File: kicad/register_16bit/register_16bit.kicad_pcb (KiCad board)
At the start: 2 copper layers, 175.3 x 72.4 mm, 84 parts, among them J1 DB37_Male, U1 SN74ALVC00, U10 SN74ALVC00, U11 SN74ALVC00, U12 SN74ALVC00, U13 SN74ALVC00, U14 SN74ALVC00, U15 SN74ALVC00, U16 SN74ALVC00, U17 SN74ALVC00, U18 SN74ALVC00, U19 SN74ALVC00, U2 SN74ALVC00, U20 SN74ALVC00, U21 SN74ALVC00, U22 SN74ALVC00, U23 SN74ALVC00, U24 SN74ALVC00, U25 SN74ALVC00, U26 SN74ALVC00, U27 SN74ALVC00, U28 SN74ALVC00, U29 SN74ALVC00, U3 SN74ALVC00, U30 SN74ALVC00, U31 SN74ALVC00, U32 SN74ALVC00, U33 SN74ALVC00, U34 SN74ALVC00, U35 SN74ALVC00, U36 SN74ALVC00, U37 SN74ALVC00, U38 SN74ALVC00, U39 SN74ALVC00, U4 SN74ALVC00, U40 SN74ALVC00, U41 SN74ALVC00, U42 SN74ALVC00, U43 SN74ALVC00, U44 SN74ALVC00, U45 SN74ALVC00, U46 SN74ALVC00, U47 SN74ALVC00, U48 SN74ALVC00, U49 SN74ALVC00, U5 SN74ALVC00, U6 SN74ALVC00, U7 SN74ALVC00, U8 SN74ALVC00, U9 SN74ALVC00

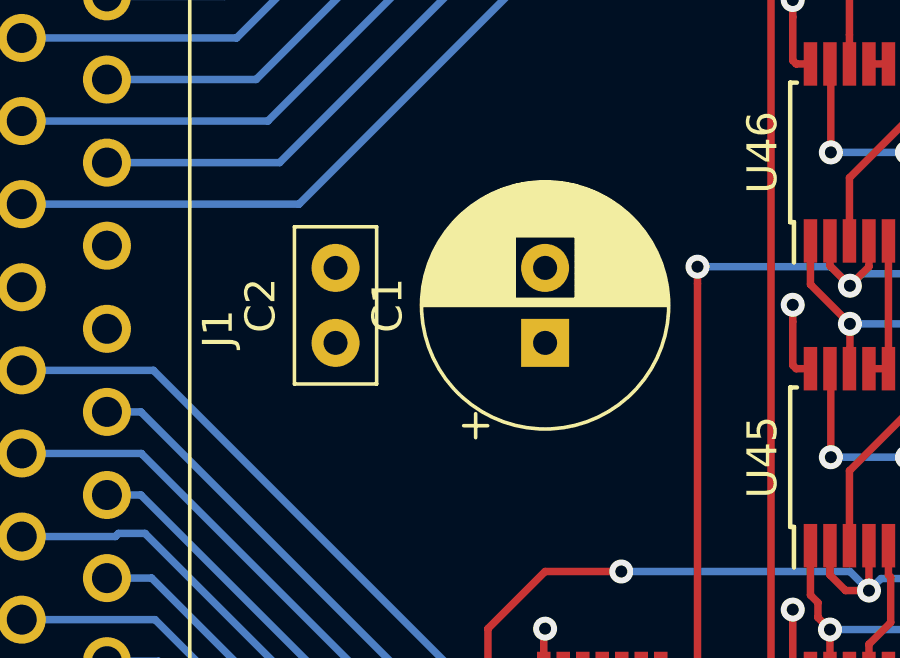
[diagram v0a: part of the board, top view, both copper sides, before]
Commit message: Added clock generator, tested on breadboard. Added motherboard, routing unfinished. Various component updates.
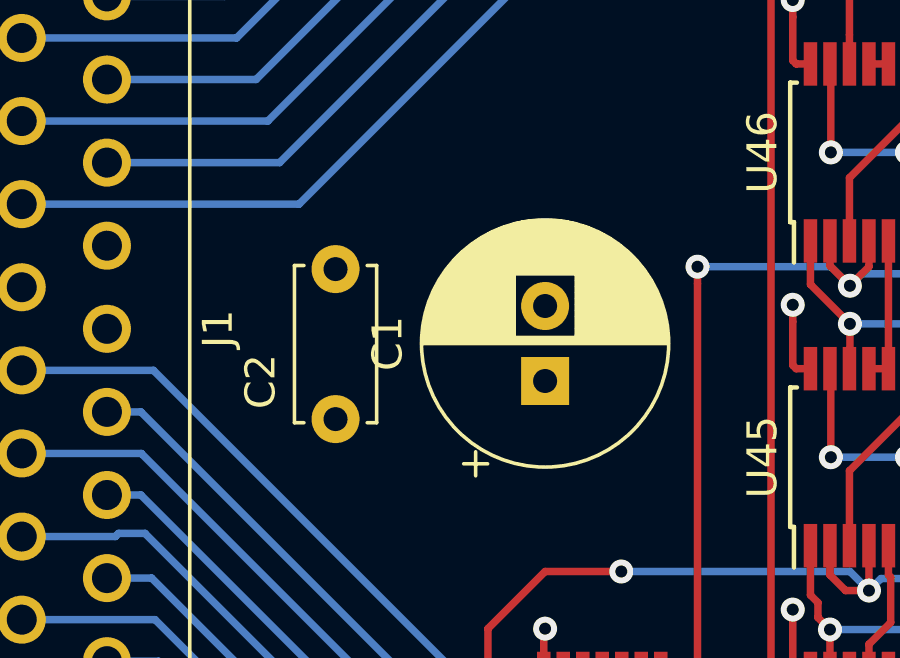
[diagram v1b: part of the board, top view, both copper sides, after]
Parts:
- C2: footprint Capacitor_THT:C_Disc_D5.0mm_W2.5mm_P2.50mm -> Capacitor_THT:C_Disc_D5.0mm_W2.5mm_P5.00mm
- moved C2 2.54 mm to (81.3, 100.3)
- moved C1 1.27 mm to (88.3, 99.1)

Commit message: ALU schematic, layout, routing complete. Associated motherboardmod. Also added Load LED to register and program counter boards.
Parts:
- added D17: LED, LED_THT:LED_D5.0mm, F.Cu at (86.4, 78.7)
- added R17: R, Resistor_SMD:R_1206_3216Metric, F.Cu at (81.9, 80.6)
- C1: value CP1 -> 100uF
- C2: value C -> 100nF
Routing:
- net load: track 215.4 -> 277.6 mm, vias 16 -> 17
- net Net-(D17-Pad1): track 0.00 -> 4.65 mm
- net out14: track 95.0 -> 96.7 mm
- net out13: track 107.3 -> 108.6 mm
- net out12: track 113.7 -> 114.7 mm
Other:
- board text added: "1"
- board text added: "10"
- board text added: "13"
- board text added: "14"
- board text added: "2"
- board text added: "5"
- board text added: "6"
- board text added: "9"
- board text added: "load"

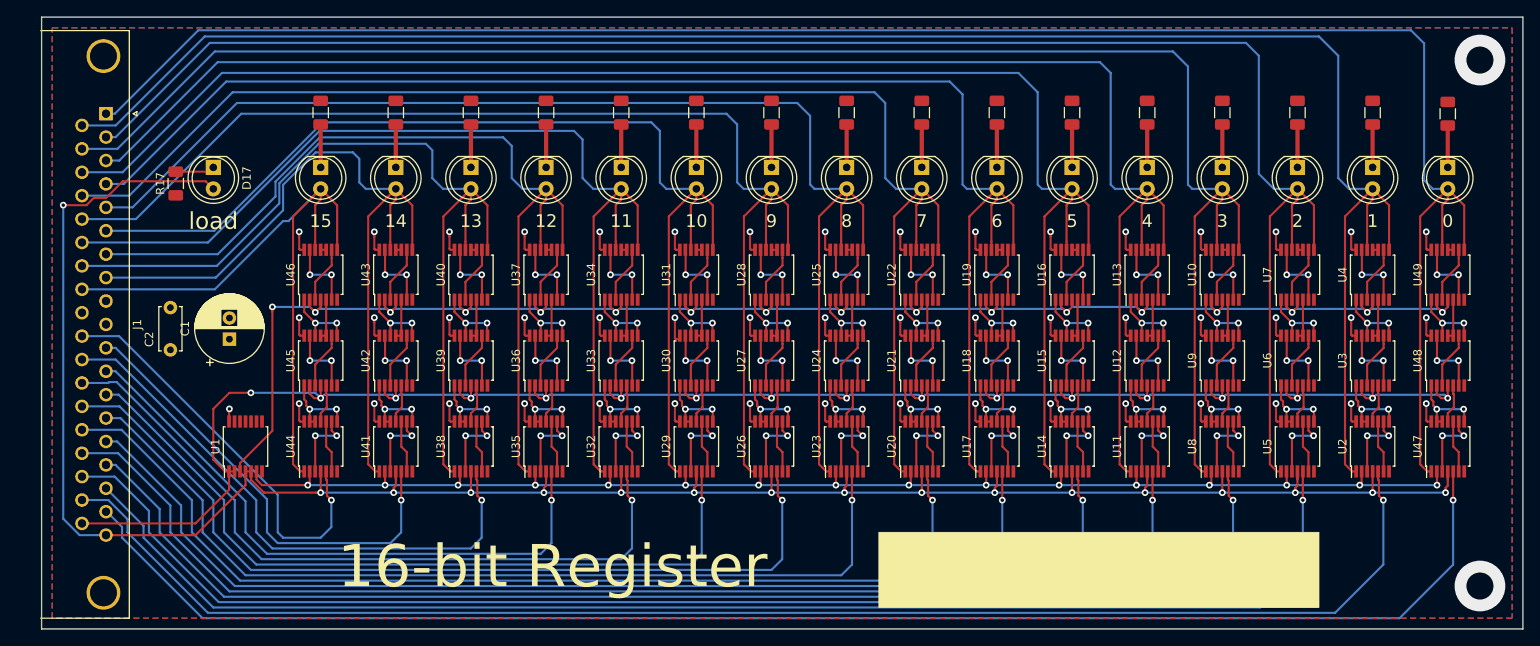
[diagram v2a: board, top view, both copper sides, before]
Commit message: Readme updates (#6)
* Readme intro section

* Board revisions for manufacturing, add digikey PNs to all, added logo.
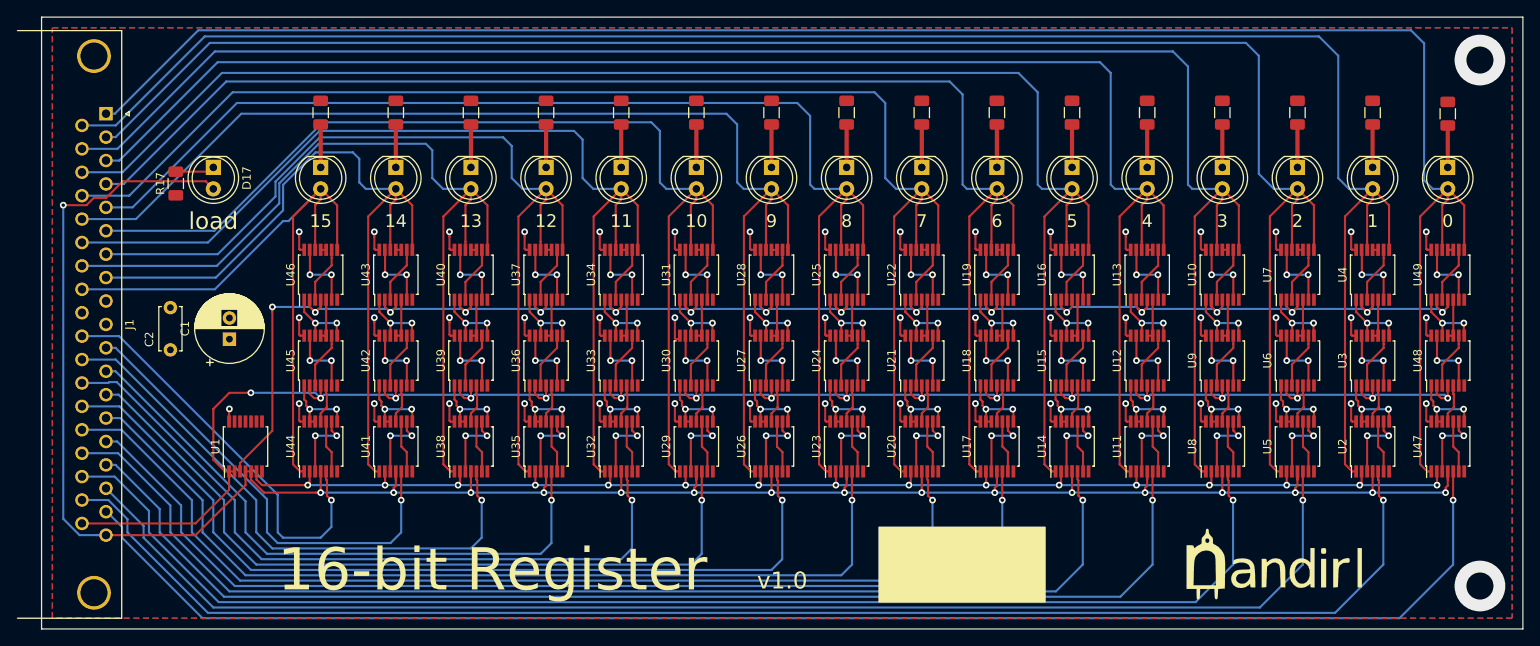
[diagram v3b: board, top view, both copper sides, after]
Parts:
- added G***: LOGO, nandirl logo:logo_sm, F.Cu at (212.1, 125.7)
- J1: footprint Connector_Dsub:DSUB-37_Male_Horizontal_P2.77x2.84mm_EdgePinOffset4.94mm_Housed_MountingHolesOffset7.48mm -> Connector_Dsub:DSUB-37_Male_Horizontal_P2.77x2.84mm_EdgePinOffset7.70mm_Housed_MountingHolesOffset9.12mm
- R1, R10, R11, R12, R13, R14, R15, R16, R17, R2, R3, R4, R5, R6, R7, R8, R9: value R -> 1K
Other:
- board text added: "v1.0"
